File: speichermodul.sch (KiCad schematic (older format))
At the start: 65 parts, among them IC1 6116, P1 CONN_3X2, P2 CONN_01X01, P3 CONN_01X01, P4 CONN_01X01, P5 CONN_01X01, P6 CONN_01X01, P7 CONN_01X01, P8 CONN_02X10, P9 CONN_02X10, SW1 SW_PUSH, SW2 SW_PUSH, U1 7400, U2 74LS08, U3 74LS08, U4 74LS14, U5 74LS540, U6 74LS540

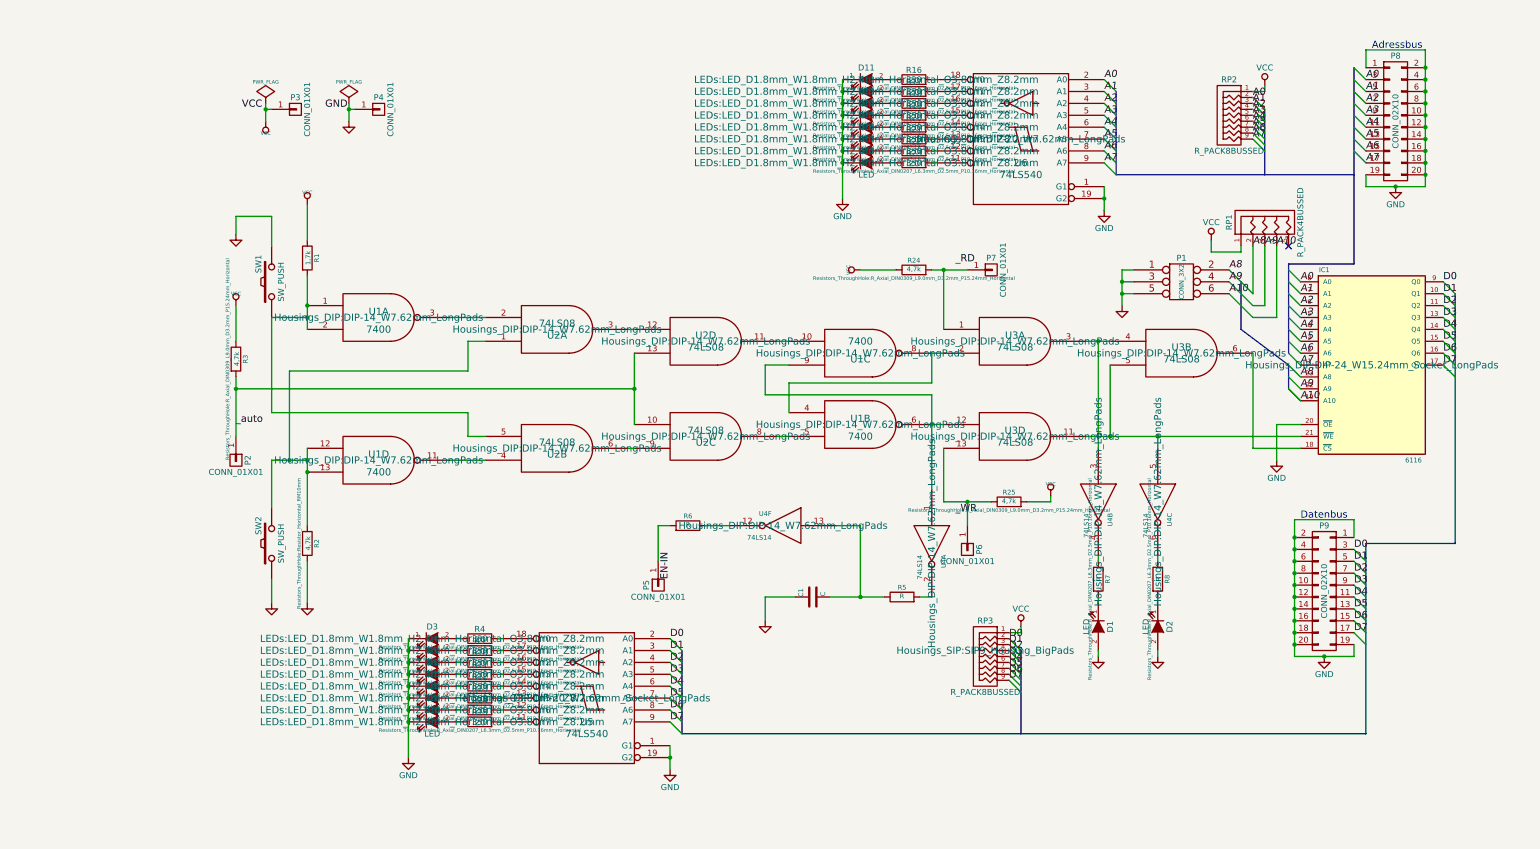
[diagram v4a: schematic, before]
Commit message: Pcb layout perfektioniert und schaltplan vorangetrieben
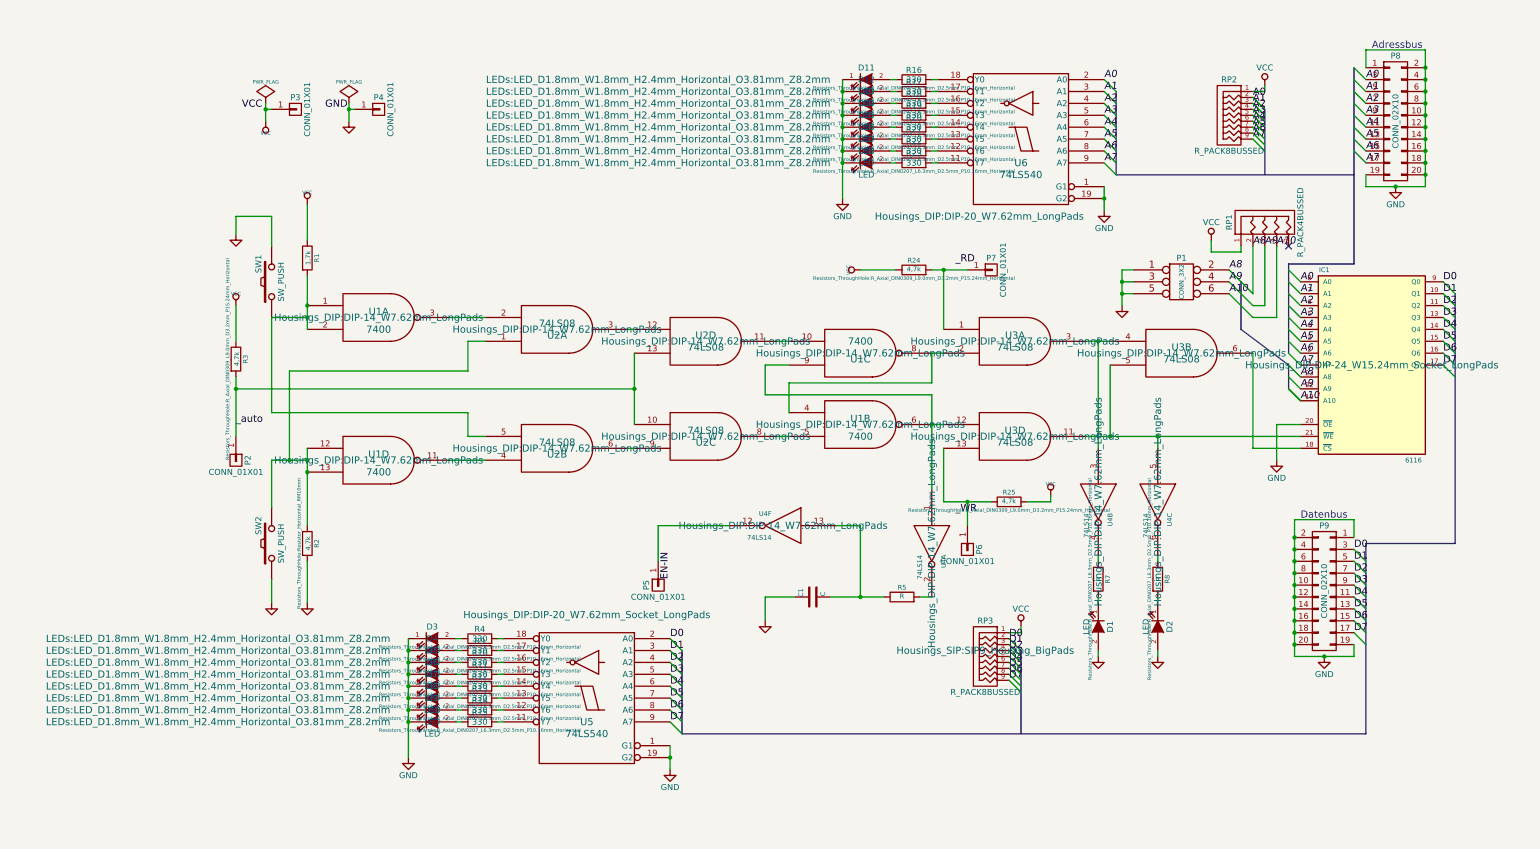
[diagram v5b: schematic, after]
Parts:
- removed R6: R, symbol R
- D1, D2: footprint LEDs:LED-3MM -> LEDs:LED_D3.0mm
- P2, P5, P6: footprint (none) -> Pin_Headers:Pin_Header_Straight_1x01_Pitch1.27mm
- P7: footprint Housings_DIP:DIP-16_W7.62mm -> Pin_Headers:Pin_Header_Straight_1x01_Pitch1.27mm
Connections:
- net at U4.12: now also P5.1 (P1)
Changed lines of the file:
@@
-$EndComp
-$Comp
-L R R6
-U 1 1 57D2D83F
-P 4500 4700
-F 0 "R6" V 4580 4700 40  0000 C CNN
-F 1 "R" V 4507 4701 40  0000 C CNN
-F 2 "" V 4430 4700 30  0001 C CNN
-F 3 "~" H 4500 4700 30  0000 C CNN
-	1    4500 4700
-	0    1    -1   0
 $EndComp
 $Comp
@@
 F 0 "D1" H 7950 5650 50  0000 C CNN
 F 1 "LED" H 7950 5450 50  0000 C CNN
-F 2 "LEDs:LED-3MM" H 7950 5550 60  0001 C CNN
+F 2 "LEDs:LED_D3.0mm" H 7950 5550 60  0001 C CNN
 F 3 "~" H 7950 5550 60  0000 C CNN
 	1    7950 5550
@@
 F 0 "D2" H 8450 5650 50  0000 C CNN
 F 1 "LED" H 8450 5450 50  0000 C CNN
-F 2 "LEDs:LED-3MM" H 8450 5550 60  0001 C CNN
+F 2 "LEDs:LED_D3.0mm" H 8450 5550 60  0001 C CNN
 F 3 "~" H 8450 5550 60  0000 C CNN
 	1    8450 5550
@@
 F 0 "P5" H 4250 5300 50  0000 C CNN
 F 1 "CONN_01X01" V 4350 5200 50  0000 C CNN
-F 2 "" H 4250 5200 60  0001 C CNN
+F 2 "Pin_Headers:Pin_Header_Straight_1x01_Pitch1.27mm" H 4250 5200 60  0001 C CNN
 F 3 "" H 4250 5200 60  0000 C CNN
 	1    4250 5200
@@
 F 0 "P6" H 6850 5000 50  0000 C CNN
 F 1 "CONN_01X01" V 6950 4900 50  0000 C CNN
-F 2 "" H 6850 4900 60  0001 C CNN
+F 2 "Pin_Headers:Pin_Header_Straight_1x01_Pitch1.27mm" H 6850 4900 60  0001 C CNN
 F 3 "" H 6850 4900 60  0000 C CNN
 	1    6850 4900
@@
 F 0 "P2" H 700 4250 50  0000 C CNN
 F 1 "CONN_01X01" V 800 4150 50  0000 C CNN
-F 2 "" H 700 4150 60  0001 C CNN
+F 2 "Pin_Headers:Pin_Header_Straight_1x01_Pitch1.27mm" H 700 4150 60  0001 C CNN
 F 3 "" H 700 4150 60  0000 C CNN
 	1    700  4150
@@
 F 0 "U6" H 7300 1250 60  0000 C CNN
 F 1 "74LS540" H 7300 1150 60  0000 C CNN
-F 2 "Housings_DIP:DIP-20_W7.62mm_LongPads" H 7300 1450 60  0000 C CNN
+F 2 "Housings_DIP:DIP-20_W7.62mm_LongPads" H 7650 800 60  0000 C CNN
 F 3 "" H 7300 1450 60  0000 C CNN
 	1    7300 1450
@@
 F 0 "U5" H 3650 5950 60  0000 C CNN
 F 1 "74LS540" H 3650 5850 60  0000 C CNN
-F 2 "Housings_DIP:DIP-20_W7.62mm_Socket_LongPads" H 3650 6150 60  0000 C CNN
+F 2 "Housings_DIP:DIP-20_W7.62mm_Socket_LongPads" H 3650 6850 60  0000 C CNN
 F 3 "" H 3650 6150 60  0000 C CNN
 	1    3650 6150
@@
 F 0 "D3" H 2350 5750 50  0000 C CNN
 F 1 "LED" H 2350 5550 50  0000 C CNN
-F 2 "LEDs:LED_D1.8mm_W1.8mm_H2.4mm_Horizontal_O3.81mm_Z8.2mm" H 2350 5650 60  0000 C CNN
+F 2 "LEDs:LED_D1.8mm_W1.8mm_H2.4mm_Horizontal_O3.81mm_Z8.2mm" H 550 5650 60  0000 C CNN
 F 3 "" H 2350 5650 60  0000 C CNN
 	1    2350 5650
@@
 F 0 "D4" H 2350 5850 50  0000 C CNN
 F 1 "LED" H 2350 5650 50  0000 C CNN
-F 2 "LEDs:LED_D1.8mm_W1.8mm_H2.4mm_Horizontal_O3.81mm_Z8.2mm" H 2350 5750 60  0000 C CNN
+F 2 "LEDs:LED_D1.8mm_W1.8mm_H2.4mm_Horizontal_O3.81mm_Z8.2mm" H 550 5750 60  0000 C CNN
 F 3 "" H 2350 5750 60  0000 C CNN
 	1    2350 5750
@@
 F 0 "D5" H 2350 5950 50  0000 C CNN
 F 1 "LED" H 2350 5750 50  0000 C CNN
-F 2 "LEDs:LED_D1.8mm_W1.8mm_H2.4mm_Horizontal_O3.81mm_Z8.2mm" H 2350 5850 60  0000 C CNN
+F 2 "LEDs:LED_D1.8mm_W1.8mm_H2.4mm_Horizontal_O3.81mm_Z8.2mm" H 550 5850 60  0000 C CNN
 F 3 "" H 2350 5850 60  0000 C CNN
 	1    2350 5850
@@
 F 0 "D6" H 2350 6050 50  0000 C CNN
 F 1 "LED" H 2350 5850 50  0000 C CNN
-F 2 "LEDs:LED_D1.8mm_W1.8mm_H2.4mm_Horizontal_O3.81mm_Z8.2mm" H 2350 5950 60  0000 C CNN
+F 2 "LEDs:LED_D1.8mm_W1.8mm_H2.4mm_Horizontal_O3.81mm_Z8.2mm" H 550 5950 60  0000 C CNN
 F 3 "" H 2350 5950 60  0000 C CNN
 	1    2350 5950
@@
 F 0 "D7" H 2350 6150 50  0000 C CNN
 F 1 "LED" H 2350 5950 50  0000 C CNN
-F 2 "LEDs:LED_D1.8mm_W1.8mm_H2.4mm_Horizontal_O3.81mm_Z8.2mm" H 2350 6050 60  0000 C CNN
+F 2 "LEDs:LED_D1.8mm_W1.8mm_H2.4mm_Horizontal_O3.81mm_Z8.2mm" H 550 6050 60  0000 C CNN
 F 3 "" H 2350 6050 60  0000 C CNN
 	1    2350 6050
@@
 F 0 "D8" H 2350 6250 50  0000 C CNN
 F 1 "LED" H 2350 6050 50  0000 C CNN
-F 2 "LEDs:LED_D1.8mm_W1.8mm_H2.4mm_Horizontal_O3.81mm_Z8.2mm" H 2350 6150 60  0000 C CNN
+F 2 "LEDs:LED_D1.8mm_W1.8mm_H2.4mm_Horizontal_O3.81mm_Z8.2mm" H 550 6150 60  0000 C CNN
 F 3 "" H 2350 6150 60  0000 C CNN
 	1    2350 6150
@@
 F 0 "D9" H 2350 6350 50  0000 C CNN
 F 1 "LED" H 2350 6150 50  0000 C CNN
-F 2 "LEDs:LED_D1.8mm_W1.8mm_H2.4mm_Horizontal_O3.81mm_Z8.2mm" H 2350 6250 60  0000 C CNN
+F 2 "LEDs:LED_D1.8mm_W1.8mm_H2.4mm_Horizontal_O3.81mm_Z8.2mm" H 550 6250 60  0000 C CNN
 F 3 "" H 2350 6250 60  0000 C CNN
 	1    2350 6250
@@
 F 0 "D10" H 2350 6450 50  0000 C CNN
 F 1 "LED" H 2350 6250 50  0000 C CNN
-F 2 "LEDs:LED_D1.8mm_W1.8mm_H2.4mm_Horizontal_O3.81mm_Z8.2mm" H 2350 6350 60  0000 C CNN
+F 2 "LEDs:LED_D1.8mm_W1.8mm_H2.4mm_Horizontal_O3.81mm_Z8.2mm" H 550 6350 60  0000 C CNN
 F 3 "" H 2350 6350 60  0000 C CNN
 	1    2350 6350
@@
 F 0 "D11" H 6000 1050 50  0000 C CNN
 F 1 "LED" H 6000 850 50  0000 C CNN
-F 2 "LEDs:LED_D1.8mm_W1.8mm_H2.4mm_Horizontal_O3.81mm_Z8.2mm" H 6000 950 60  0000 C CNN
+F 2 "LEDs:LED_D1.8mm_W1.8mm_H2.4mm_Horizontal_O3.81mm_Z8.2mm" H 4250 950 60  0000 C CNN
 F 3 "" H 6000 950 60  0000 C CNN
 	1    6000 950
@@
 F 0 "D12" H 6000 1150 50  0000 C CNN
 F 1 "LED" H 6000 950 50  0000 C CNN
-F 2 "LEDs:LED_D1.8mm_W1.8mm_H2.4mm_Horizontal_O3.81mm_Z8.2mm" H 6000 1050 60  0000 C CNN
+F 2 "LEDs:LED_D1.8mm_W1.8mm_H2.4mm_Horizontal_O3.81mm_Z8.2mm" H 4250 1050 60  0000 C CNN
 F 3 "" H 6000 1050 60  0000 C CNN
 	1    6000 1050
@@
 F 0 "D13" H 6000 1250 50  0000 C CNN
 F 1 "LED" H 6000 1050 50  0000 C CNN
-F 2 "LEDs:LED_D1.8mm_W1.8mm_H2.4mm_Horizontal_O3.81mm_Z8.2mm" H 6000 1150 60  0000 C CNN
+F 2 "LEDs:LED_D1.8mm_W1.8mm_H2.4mm_Horizontal_O3.81mm_Z8.2mm" H 4250 1150 60  0000 C CNN
 F 3 "" H 6000 1150 60  0000 C CNN
 	1    6000 1150
@@
 F 0 "D14" H 6000 1350 50  0000 C CNN
 F 1 "LED" H 6000 1150 50  0000 C CNN
-F 2 "LEDs:LED_D1.8mm_W1.8mm_H2.4mm_Horizontal_O3.81mm_Z8.2mm" H 6000 1250 60  0000 C CNN
+F 2 "LEDs:LED_D1.8mm_W1.8mm_H2.4mm_Horizontal_O3.81mm_Z8.2mm" H 4250 1250 60  0000 C CNN
 F 3 "" H 6000 1250 60  0000 C CNN
 	1    6000 1250
@@
 F 0 "D15" H 6000 1450 50  0000 C CNN
 F 1 "LED" H 6000 1250 50  0000 C CNN
-F 2 "LEDs:LED_D1.8mm_W1.8mm_H2.4mm_Horizontal_O3.81mm_Z8.2mm" H 6000 1350 60  0000 C CNN
+F 2 "LEDs:LED_D1.8mm_W1.8mm_H2.4mm_Horizontal_O3.81mm_Z8.2mm" H 4250 1350 60  0000 C CNN
 F 3 "" H 6000 1350 60  0000 C CNN
 	1    6000 1350
@@
 F 0 "D16" H 6000 1550 50  0000 C CNN
 F 1 "LED" H 6000 1350 50  0000 C CNN
-F 2 "LEDs:LED_D1.8mm_W1.8mm_H2.4mm_Horizontal_O3.81mm_Z8.2mm" H 6000 1450 60  0000 C CNN
+F 2 "LEDs:LED_D1.8mm_W1.8mm_H2.4mm_Horizontal_O3.81mm_Z8.2mm" H 4250 1450 60  0000 C CNN
 F 3 "" H 6000 1450 60  0000 C CNN
 	1    6000 1450
@@
 F 0 "D17" H 6000 1650 50  0000 C CNN
 F 1 "LED" H 6000 1450 50  0000 C CNN
-F 2 "LEDs:LED_D1.8mm_W1.8mm_H2.4mm_Horizontal_O3.81mm_Z8.2mm" H 6000 1550 60  0000 C CNN
+F 2 "LEDs:LED_D1.8mm_W1.8mm_H2.4mm_Horizontal_O3.81mm_Z8.2mm" H 4250 1550 60  0000 C CNN
 F 3 "" H 6000 1550 60  0000 C CNN
 	1    6000 1550
@@
 F 0 "D18" H 6000 1750 50  0000 C CNN
 F 1 "LED" H 6000 1550 50  0000 C CNN
-F 2 "LEDs:LED_D1.8mm_W1.8mm_H2.4mm_Horizontal_O3.81mm_Z8.2mm" H 6000 1650 60  0000 C CNN
+F 2 "LEDs:LED_D1.8mm_W1.8mm_H2.4mm_Horizontal_O3.81mm_Z8.2mm" H 4250 1650 60  0000 C CNN
 F 3 "" H 6000 1650 60  0000 C CNN
 	1    6000 1650
@@
 F 0 "P7" H 7050 2650 50  0000 C CNN
 F 1 "CONN_01X01" V 7150 2550 50  0000 C CNN
-F 2 "Housings_DIP:DIP-16_W7.62mm" H 7050 2550 60  0001 C CNN
+F 2 "Pin_Headers:Pin_Header_Straight_1x01_Pitch1.27mm" H 7050 2550 60  0001 C CNN
 F 3 "" H 7050 2550 60  0000 C CNN
 	1    7050 2550
@@
 Connection ~ 6550 3850
 Wire Wire Line
-	4850 4700 4650 4700
+	4250 4700 4850 4700
 Wire Wire Line
 	5150 5300 5400 5300
@@
 	6550 2550 6850 2550
 Wire Wire Line
-	4250 4700 4350 4700
-Wire Wire Line
 	9450 4150 9450 3850

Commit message: Version changegit status! footprints, pcb speichermodul
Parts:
- C1: value C -> 0; footprint (none) -> Capacitors_ThroughHole:C_Disc_D10.0mm_W2.5mm_P5.00mm; symbol C -> speichermodul-rescue:C-RESCUE-speichermodul
- D1, D10, D11, D12, D13, D14, D15, D16, D17, D18, D2, D3, D4, D5, D6, D7, D8, D9: symbol LED -> speichermodul-rescue:LED-RESCUE-speichermodul
- IC1: symbol 6116-RESCUE-speichermodul -> speichermodul-rescue:6116-RESCUE-speichermodul
- P1: footprint (none) -> Connectors_Samtec:SDL-106-X-XX_2x03; symbol CONN_3X2 -> speichermodul-rescue:CONN_3X2-RESCUE-speichermodul
- P2, P3, P4, P5, P6, P7: symbol CONN_01X01 -> speichermodul-rescue:CONN_01X01-RESCUE-speichermodul
- P8: footprint Connect:IDC_Header_Straight_20pins -> Connectors_Samtec:SDL-120-X-XX_2x10; symbol CONN_02X10 -> speichermodul-rescue:CONN_02X10-RESCUE-speichermodul
- P9: symbol CONN_02X10 -> speichermodul-rescue:CONN_02X10-RESCUE-speichermodul
- R1, R10, R11, R12, R13, R14, R15, R16, R17, R18, R19, R2, R20, R21, R22, R23, R24, R25, R3, R4, R7, R8, R9: symbol R -> speichermodul-rescue:R-RESCUE-speichermodul
- R5: value R -> 0; footprint (none) -> Resistors_ThroughHole:R_Axial_DIN0309_L9.0mm_D3.2mm_P15.24mm_Horizontal; symbol R -> speichermodul-rescue:R-RESCUE-speichermodul
- RP1: symbol R_PACK4BUSSED -> speichermodul-rescue:R_PACK4BUSSED-RESCUE-speichermodul
- RP2, RP3: symbol R_PACK8BUSSED -> speichermodul-rescue:R_PACK8BUSSED-RESCUE-speichermodul
- SW1, SW2: symbol SW_PUSH -> speichermodul-rescue:SW_PUSH-RESCUE-speichermodul
- U1: symbol 7400 -> speichermodul-rescue:7400-RESCUE-speichermodul
- U2, U3: symbol 74LS08 -> speichermodul-rescue:74LS08-RESCUE-speichermodul
- U4: symbol 74LS14 -> speichermodul-rescue:74LS14-RESCUE-speichermodul
- U5, U6: symbol 74LS540 -> speichermodul-rescue:74LS540-RESCUE-speichermodul
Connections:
- wire segments 137 -> 181

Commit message: RPacked 5Pinns in Befehle und Speicher added and some strange fixes (not connected pins ...)
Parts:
- RP1: footprint (none) -> Resistors_ThroughHole:R_Array_SIP5
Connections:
- wire segments 181 -> 207
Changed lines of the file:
@@
 F 0 "RP1" H 9350 2450 50  0000 C CNN
 F 1 "R_PACK4BUSSED" H 9350 1850 50  0000 C CNN
-F 2 "" H 9350 2000 60  0001 C CNN
+F 2 "Resistors_ThroughHole:R_Array_SIP5" H 9350 2000 60  0000 C CNN
 F 3 "" H 9350 2000 60  0000 C CNN
 	1    9350 2150
@@
 	950  1200 950  1300
 Wire Wire Line
-	1300 2600 1300 2950
-Wire Wire Line
-	8000 1850 8000 2050
-Wire Wire Line
-	4350 6550 4350 6750
-Wire Wire Line
-	10200 1850 10700 1850
-Wire Wire Line
-	9600 5800 10100 5800
-Wire Wire Line
-	1300 4150 1300 4700
-Wire Wire Line
-	10700 700  10700 1850
-Wire Wire Line
-	9600 4650 9600 5800
+	1300 2600 1300 2850
+Wire Wire Line
+	1300 4150 1300 4250
+Wire Wire Line
+	9600 5800 9850 5800
+Connection ~ 9850 5800
+Wire Wire Line
+	9850 5800 10100 5800
+Wire Wire Line
+	9600 4650 9600 4800
+Connection ~ 9600 5700
+Wire Wire Line
+	9600 5700 9600 5800
+Connection ~ 9600 4800
+Wire Wire Line
+	9600 4800 9600 4900
+Connection ~ 9600 4900
+Wire Wire Line
+	9600 4900 9600 5000
+Connection ~ 9600 5000
+Wire Wire Line
+	9600 5000 9600 5100
+Connection ~ 9600 5100
+Wire Wire Line
+	9600 5100 9600 5200
+Connection ~ 9600 5200
+Wire Wire Line
+	9600 5200 9600 5300
+Connection ~ 9600 5300
+Wire Wire Line
+	9600 5300 9600 5400
+Connection ~ 9600 5400
+Wire Wire Line
+	9600 5400 9600 5500
+Connection ~ 9600 5500
+Wire Wire Line
+	9600 5500 9600 5600
+Connection ~ 9600 5600
+Wire Wire Line
+	9600 5600 9600 5700
+Wire Wire Line
+	1300 2850 1300 2950
+Connection ~ 1300 2850
+Connection ~ 1000 2950
+Connection ~ 1300 4250
+Wire Wire Line
+	1300 4250 1300 4700
+Wire Wire Line
+	10700 700  10700 850
+Connection ~ 10700 850
+Wire Wire Line
+	10700 850  10700 950
+Connection ~ 10700 1750
+Wire Wire Line
+	10700 1750 10700 1850
+Connection ~ 10700 950
+Wire Wire Line
+	10700 950  10700 1050
+Connection ~ 10700 1050
+Wire Wire Line
+	10700 1050 10700 1150
+Connection ~ 10700 1150
+Wire Wire Line
+	10700 1150 10700 1250
+Connection ~ 10700 1250
+Wire Wire Line
+	10700 1250 10700 1350
+Connection ~ 10700 1350
+Wire Wire Line
+	10700 1350 10700 1450
+Connection ~ 10700 1450
+Wire Wire Line
+	10700 1450 10700 1550
+Connection ~ 10700 1550
+Wire Wire Line
+	10700 1550 10700 1650
+Connection ~ 10700 1650
+Wire Wire Line
+	10700 1650 10700 1750
+Wire Wire Line
+	10200 1850 10450 1850
+Connection ~ 10450 1850
+Wire Wire Line
+	10450 1850 10700 1850
+Wire Wire Line
+	4350 6550 4350 6650
+Connection ~ 4350 6650
+Wire Wire Line
+	4350 6650 4350 6750
+Wire Wire Line
+	8000 1850 8000 1950
+Wire Bus Line
+	9550 3350 9550 3550
+Wire Bus Line
+	9150 2650 9150 3050
+Wire Bus Line
+	4450 5750 4450 6450
+Wire Bus Line
+	8100 1050 8100 1750
+Wire Bus Line
+	10950 2750 10950 4850
+Wire Bus Line
+	10200 4850 10200 6450
+Wire Bus Line
+	9550 2500 9550 3250
+Wire Bus Line
+	10100 850  10100 2500
+Wire Bus Line
+	9350 1200 9350 1750
 Wire Bus Line
 	7300 5750 7300 6450
-Wire Bus Line
-	9350 1200 9350 1750
-Wire Bus Line
-	10100 850  10100 2500
-Wire Bus Line
-	9550 2500 9550 3250
-Wire Bus Line
-	10200 4850 10200 6450
-Wire Bus Line
-	10950 2750 10950 4850
-Wire Bus Line
-	8100 1050 8100 1750
-Wire Bus Line
-	4450 5750 4450 6450
-Wire Bus Line
-	9150 2650 9150 3050
-Wire Bus Line
-	9550 3350 9550 3550
+Connection ~ 8000 1950
+Wire Wire Line
+	8000 1950 8000 2050
 $EndSCHEMATC
